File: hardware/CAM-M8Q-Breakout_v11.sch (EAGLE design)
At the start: 24 parts, among them J2 MA06-1, J3 MA06-1, X1 PASSER-07, X2 PASSER-07, X3 PASSER-07, X4 PASSER-07

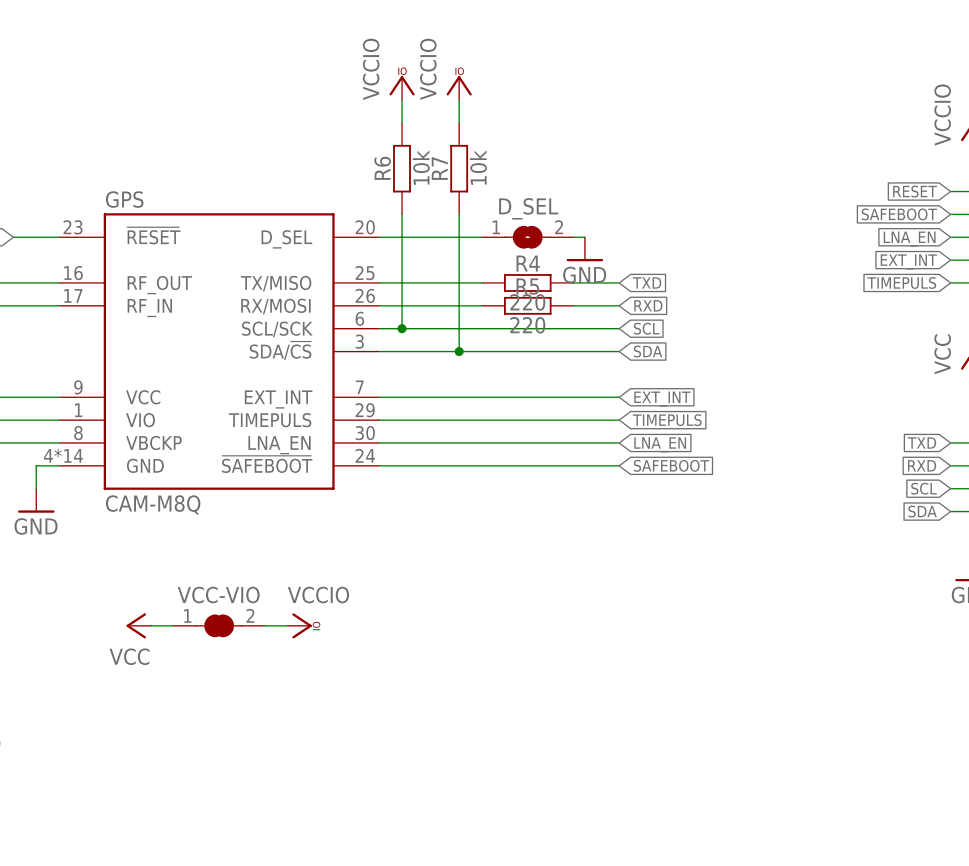
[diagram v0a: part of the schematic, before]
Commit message: updated schematics
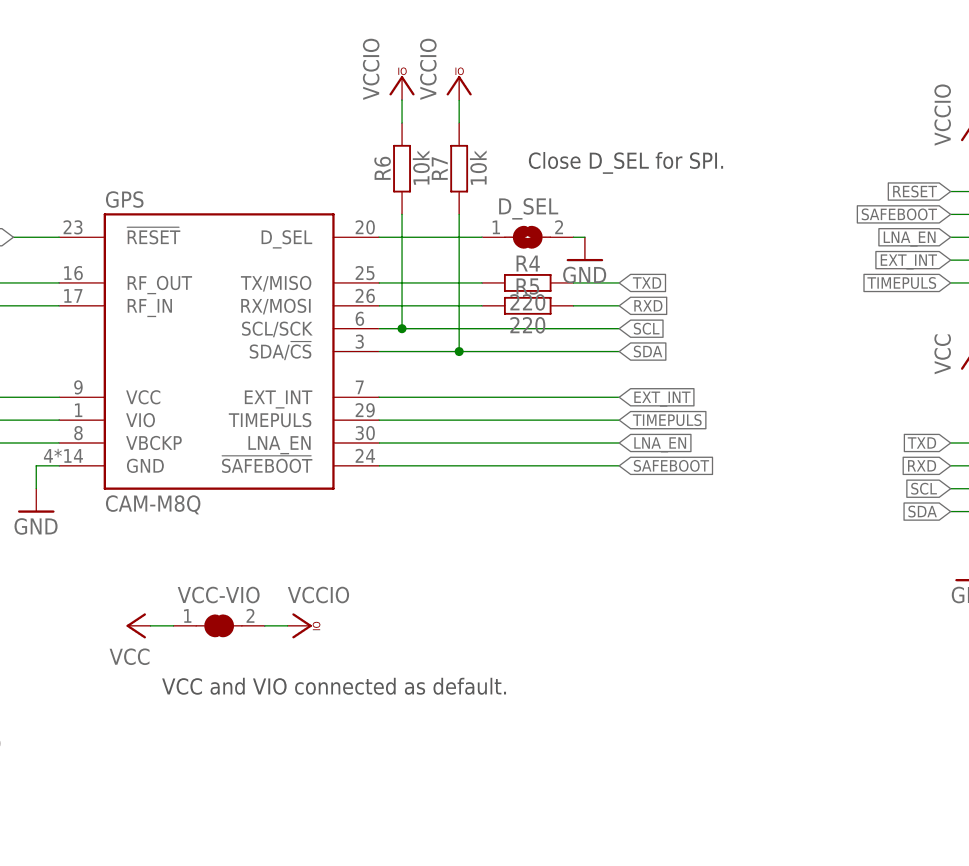
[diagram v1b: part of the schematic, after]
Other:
- note added: "Close D_SEL for SPI."
- note added: "VCC and VIO connected as default."
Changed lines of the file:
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@@
 <grid distance="0.05" unitdist="inch" unit="inch" style="lines" multiple="1" display="yes" altdistance="0.01" altunitdist="inch" altunit="inch"/>
 <layers>
-<layer number="1" name="Top" color="4" fill="1" visible="yes" active="no"/>
-<layer number="2" name="Route2" color="1" fill="3" visible="yes" active="no"/>
-<layer number="3" name="Route3" color="4" fill="3" visible="yes" active="no"/>
-<layer number="4" name="Route4" color="1" fill="4" visible="yes" active="no"/>
-<layer number="5" name="Route5" color="4" fill="4" visible="yes" active="no"/>
-<layer number="6" name="Route6" color="1" fill="8" visible="yes" active="no"/>
-<layer number="7" name="Route7" color="4" fill="8" visible="yes" active="no"/>
-<layer number="8" name="Route8" color="1" fill="2" visible="yes" active="no"/>
-<layer number="9" name="Route9" color="4" fill="2" visible="yes" active="no"/>
-<layer number="10" name="Route10" color="1" fill="7" visible="yes" active="no"/>
-<layer number="11" name="Route11" color="4" fill="7" visible="yes" active="no"/>
-<layer number="12" name="Route12" color="1" fill="5" visible="yes" active="no"/>
-<layer number="13" name="Route13" color="4" fill="5" visible="yes" active="no"/>
-<layer number="14" name="Route14" color="1" fill="6" visible="yes" active="no"/>
-<layer number="15" name="Route15" color="4" fill="6" visible="yes" active="no"/>
-<layer number="16" name="Bottom" color="1" fill="1" visible="yes" active="no"/>
-<layer number="17" name="Pads" color="2" fill="1" visible="yes" active="no"/>
-<layer number="18" name="Vias" color="2" fill="1" visible="yes" active="no"/>
-<layer number="19" name="Unrouted" color="6" fill="1" visible="yes" active="no"/>
-<layer number="20" name="Dimension" color="15" fill="1" visible="yes" active="no"/>
-<layer number="21" name="tPlace" color="7" fill="1" visible="yes" active="no"/>
-<layer number="22" name="bPlace" color="7" fill="1" visible="yes" active="no"/>
-<layer number="23" name="tOrigins" color="15" fill="1" visible="yes" active="no"/>
-<layer number="24" name="bOrigins" color="15" fill="1" visible="yes" active="no"/>
-<layer number="25" name="tNames" color="7" fill="1" visible="yes" active="no"/>
-<layer number="26" name="bNames" color="7" fill="1" visible="yes" active="no"/>
-<layer number="27" name="tValues" color="7" fill="1" visible="yes" active="no"/>
-<layer number="28" name="bValues" color="7" fill="1" visible="yes" active="no"/>
+<layer number="1" name="Top" color="4" fill="1" visible="no" active="no"/>
+<layer number="2" name="Route2" color="1" fill="3" visible="no" active="no"/>
+<layer number="3" name="Route3" color="4" fill="3" visible="no" active="no"/>
+<layer number="4" name="Route4" color="1" fill="4" visible="no" active="no"/>
+<layer number="5" name="Route5" color="4" fill="4" visible="no" active="no"/>
+<layer number="6" name="Route6" color="1" fill="8" visible="no" active="no"/>
+<layer number="7" name="Route7" color="4" fill="8" visible="no" active="no"/>
+<layer number="8" name="Route8" color="1" fill="2" visible="no" active="no"/>
+<layer number="9" name="Route9" color="4" fill="2" visible="no" active="no"/>
+<layer number="10" name="Route10" color="1" fill="7" visible="no" active="no"/>
+<layer number="11" name="Route11" color="4" fill="7" visible="no" active="no"/>
+<layer number="12" name="Route12" color="1" fill="5" visible="no" active="no"/>
+<layer number="13" name="Route13" color="4" fill="5" visible="no" active="no"/>
+<layer number="14" name="Route14" color="1" fill="6" visible="no" active="no"/>
+<layer number="15" name="Route15" color="4" fill="6" visible="no" active="no"/>
+<layer number="16" name="Bottom" color="1" fill="1" visible="no" active="no"/>
+<layer number="17" name="Pads" color="2" fill="1" visible="no" active="no"/>
+<layer number="18" name="Vias" color="2" fill="1" visible="no" active="no"/>
+<layer number="19" name="Unrouted" color="6" fill="1" visible="no" active="no"/>
+<layer number="20" name="Dimension" color="15" fill="1" visible="no" active="no"/>
+<layer number="21" name="tPlace" color="7" fill="1" visible="no" active="no"/>
+<layer number="22" name="bPlace" color="7" fill="1" visible="no" active="no"/>
+<layer number="23" name="tOrigins" color="15" fill="1" visible="no" active="no"/>
+<layer number="24" name="bOrigins" color="15" fill="1" visible="no" active="no"/>
+<layer number="25" name="tNames" color="7" fill="1" visible="no" active="no"/>
+<layer number="26" name="bNames" color="7" fill="1" visible="no" active="no"/>
+<layer number="27" name="tValues" color="7" fill="1" visible="no" active="no"/>
+<layer number="28" name="bValues" color="7" fill="1" visible="no" active="no"/>
 <layer number="29" name="tStop" color="7" fill="3" visible="no" active="no"/>
 <layer number="30" name="bStop" color="7" fill="6" visible="no" active="no"/>
@@
 <layer number="35" name="tGlue" color="7" fill="4" visible="no" active="no"/>
 <layer number="36" name="bGlue" color="7" fill="5" visible="no" active="no"/>
-<layer number="37" name="tTest" color="7" fill="1" visible="yes" active="no"/>
-<layer number="38" name="bTest" color="7" fill="1" visible="yes" active="no"/>
+<layer number="37" name="tTest" color="7" fill="1" visible="no" active="no"/>
+<layer number="38" name="bTest" color="7" fill="1" visible="no" active="no"/>
 <layer number="39" name="tKeepout" color="4" fill="11" visible="no" active="no"/>
 <layer number="40" name="bKeepout" color="1" fill="11" visible="no" active="no"/>
@@
 <layer number="44" name="Drills" color="7" fill="1" visible="no" active="no"/>
 <layer number="45" name="Holes" color="7" fill="1" visible="no" active="no"/>
-<layer number="46" name="Milling" color="3" fill="1" visible="yes" active="no"/>
-<layer number="47" name="Measures" color="7" fill="1" visible="yes" active="no"/>
-<layer number="48" name="Document" color="7" fill="1" visible="yes" active="no"/>
-<layer number="49" name="Reference" color="7" fill="1" visible="yes" active="no"/>
-<layer number="50" name="dxf" color="7" fill="1" visible="yes" active="no"/>
-<layer number="51" name="tDocu" color="7" fill="1" visible="yes" active="no"/>
-<layer number="52" name="bDocu" color="7" fill="1" visible="yes" active="no"/>
+<layer number="46" name="Milling" color="3" fill="1" visible="no" active="no"/>
+<layer number="47" name="Measures" color="7" fill="1" visible="no" active="no"/>
+<layer number="48" name="Document" color="7" fill="1" visible="no" active="no"/>
+<layer number="49" name="Reference" color="7" fill="1" visible="no" active="no"/>
+<layer number="50" name="dxf" color="7" fill="1" visible="no" active="no"/>
+<layer number="51" name="tDocu" color="7" fill="1" visible="no" active="no"/>
+<layer number="52" name="bDocu" color="7" fill="1" visible="no" active="no"/>
 <layer number="90" name="Modules" color="5" fill="1" visible="yes" active="yes"/>
 <layer number="91" name="Nets" color="2" fill="1" visible="yes" active="yes"/>
@@
 Designed by Watterott electronic</text>
 <wire x1="114.935" y1="73.66" x2="116.205" y2="73.66" width="0.4064" layer="94"/>
+<text x="149.86" y="124.46" size="1.778" layer="97">Close D_SEL for SPI.</text>
+<text x="109.22" y="66.04" size="1.778" layer="97">VCC and VIO connected as default.</text>
 </plain>
 <instances>
